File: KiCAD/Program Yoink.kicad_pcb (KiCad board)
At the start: 2 copper layers, 257.2 x 83.3 mm, 123 parts, among them SW1 Rotary_Encoder_Switch, SW2 SW_Push, U1 ATmega32U2-AU, U2 PRTR5V0U2X, Y1 Crystal_GND24_Small

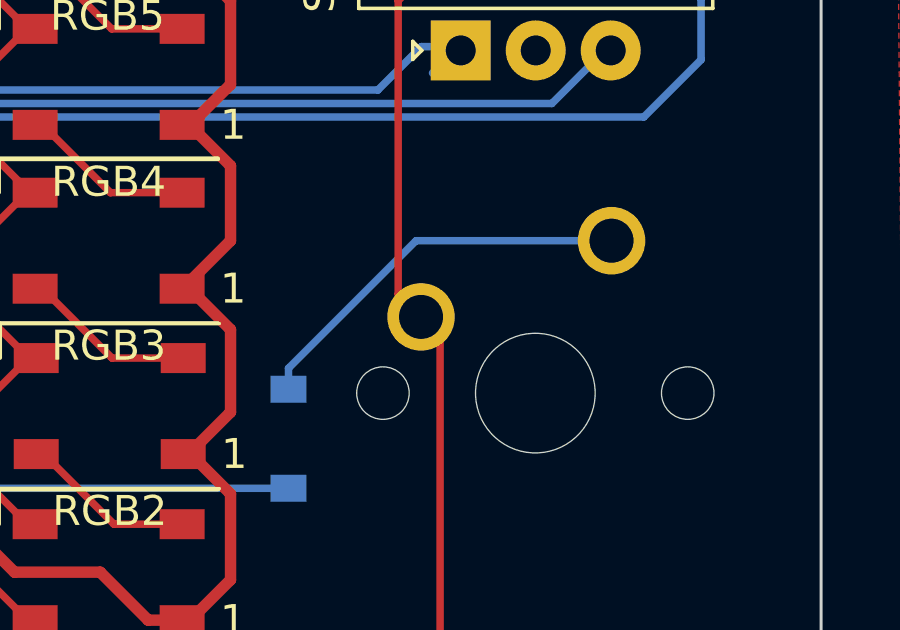
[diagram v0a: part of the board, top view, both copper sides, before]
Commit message: Updated Symbol lib path
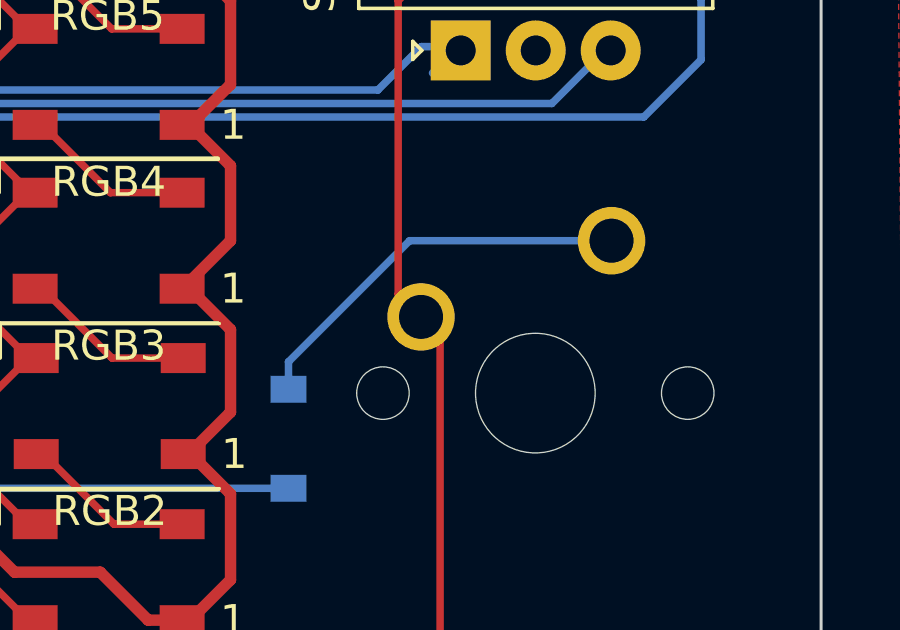
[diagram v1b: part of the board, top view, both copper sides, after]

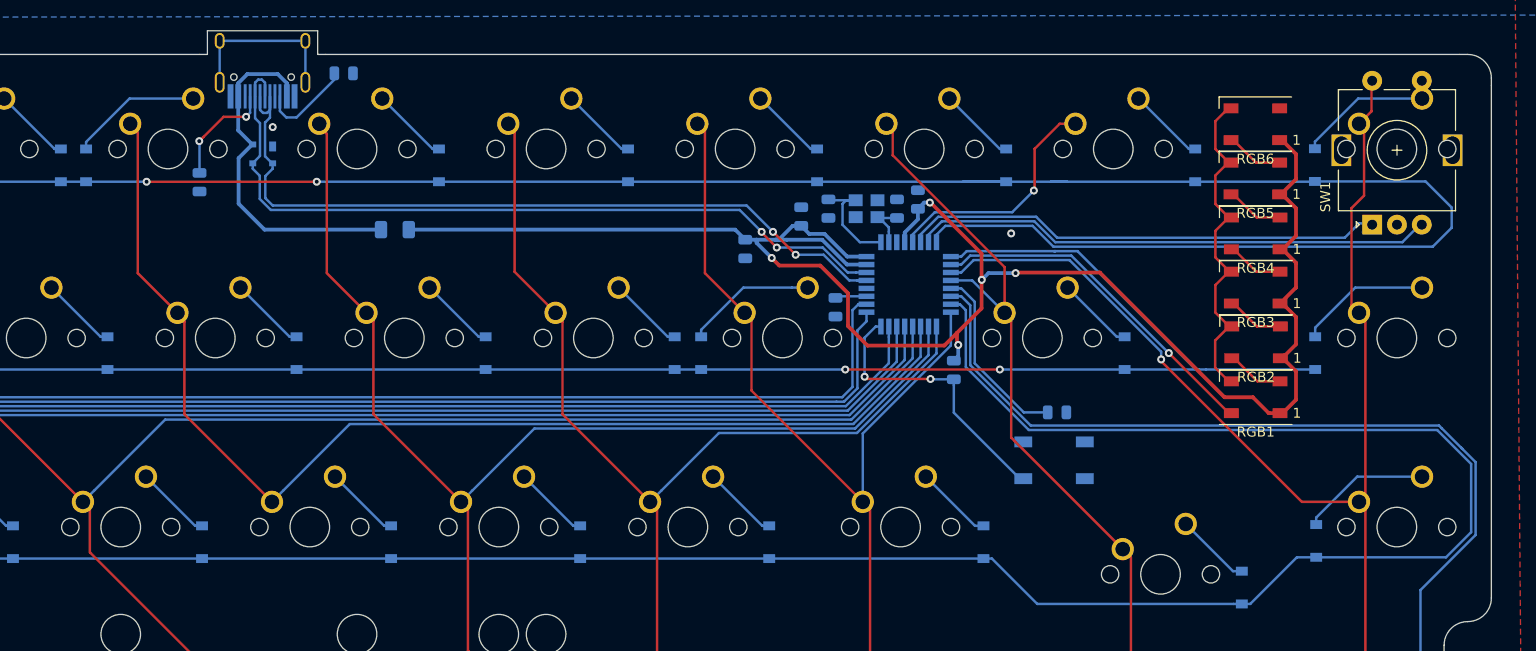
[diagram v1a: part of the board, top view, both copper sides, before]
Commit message: Fixed LED gnd
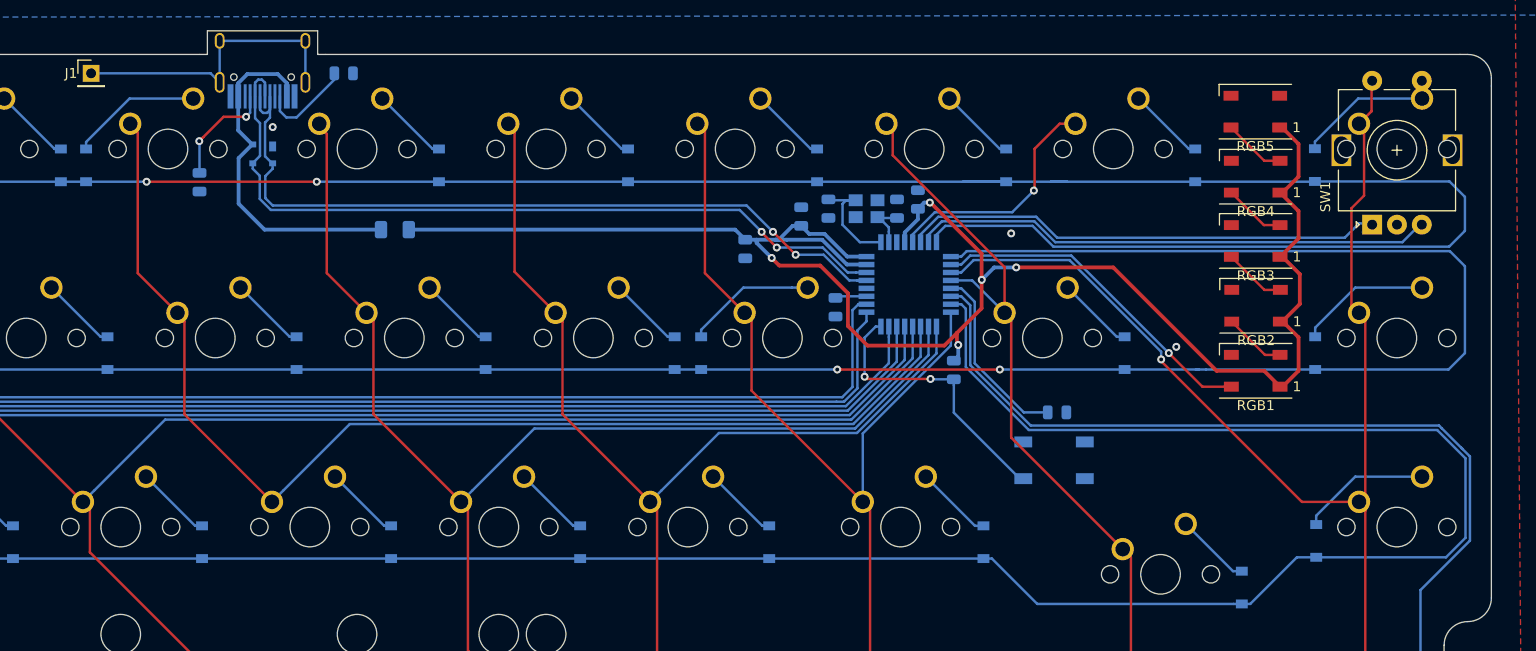
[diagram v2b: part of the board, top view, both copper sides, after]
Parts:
- removed RGB6: WS2812B, LED_SMD:LED_WS2812B_PLCC4_5.0x5.0mm_P3.2mm
- added G***: LOGO, Silk:Program_Yoink_silk_400, F.Cu at (-5.08, -221.1)
- added G***: LOGO, Silk:Program_Yoink_silk_100, F.Cu at (-17.4, -317.0)
- added J1: Conn_01x01, Connector_PinHeader_2.54mm:PinHeader_1x01_P2.54mm_Vertical, F.Cu at (-20.4, -258.4)
- moved RGB5 6.73 mm to (96.9, -254.6)
- moved RGB4 5.72 mm to (96.9, -248.0)
- moved RGB3 4.70 mm to (96.9, -241.6)
- moved RGB2 3.68 mm to (96.9, -235.0)
- moved RGB1 2.67 mm to (96.9, -228.5)
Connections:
- RGB1 pad 3: Net-(RGB1-Pad3) -> GND
- RGB2 pad 3: Net-(RGB1-Pad3) -> GND
- RGB3 pad 3: Net-(RGB1-Pad3) -> GND
- RGB4 pad 3: Net-(RGB1-Pad3) -> GND
- RGB5 pad 3: Net-(RGB1-Pad3) -> GND
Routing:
- net ROW01: track 249.3 -> 296.5 mm
- net Net-(RGB1-Pad3): track 35.4 -> 0.00 mm
- net Net-(J1-Pad1): track 17.0 -> 30.3 mm
- net Net-(RGB5-Pad2): track 5.84 -> 0.00 mm
- net ROW00: track 298.8 -> 302.3 mm
- net +5V: track 183.1 -> 180.6 mm
- net GND: track 0.00 -> 1.00 mm, vias 2 -> 3
- net RGB_PWM: track 35.2 -> 34.4 mm
- net Net-(RGB2-Pad2): track 5.89 -> 6.57 mm
- net Net-(RGB4-Pad2): track 5.91 -> 6.58 mm
- net Net-(RGB3-Pad2): track 5.84 -> 6.51 mm
- net Net-(RGB1-Pad2): track 5.83 -> 6.50 mm
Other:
- board text removed: "PROGRAM YOINK!"

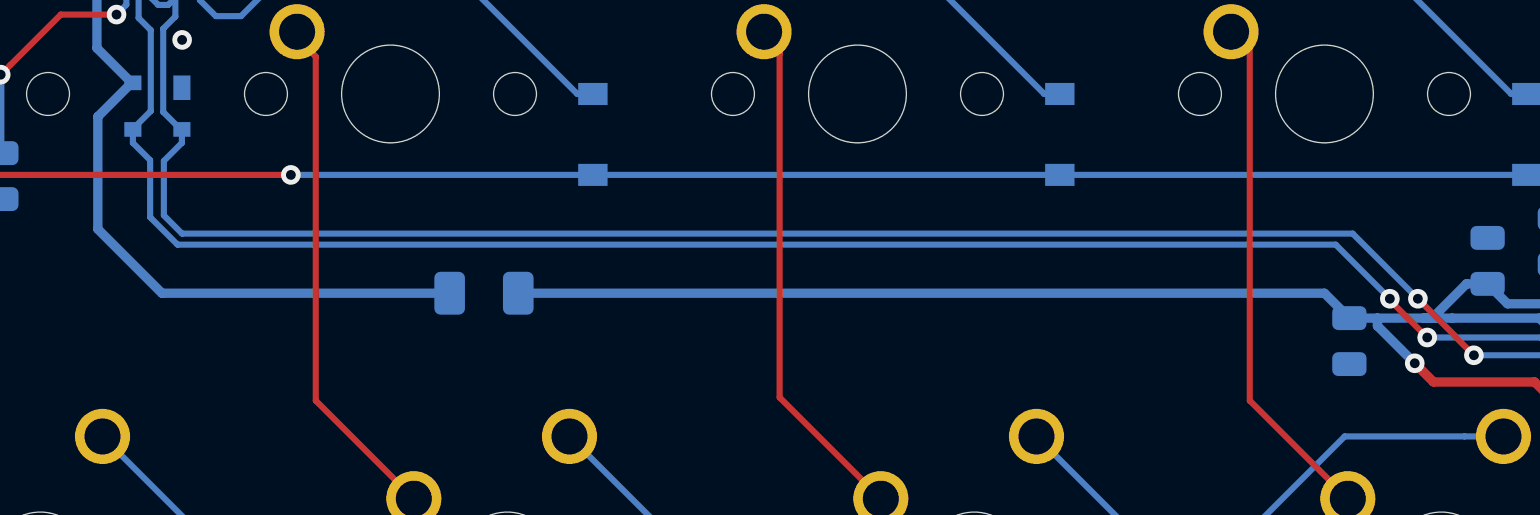
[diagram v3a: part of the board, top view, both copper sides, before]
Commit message: Updated PCB
Added resistors to data lines
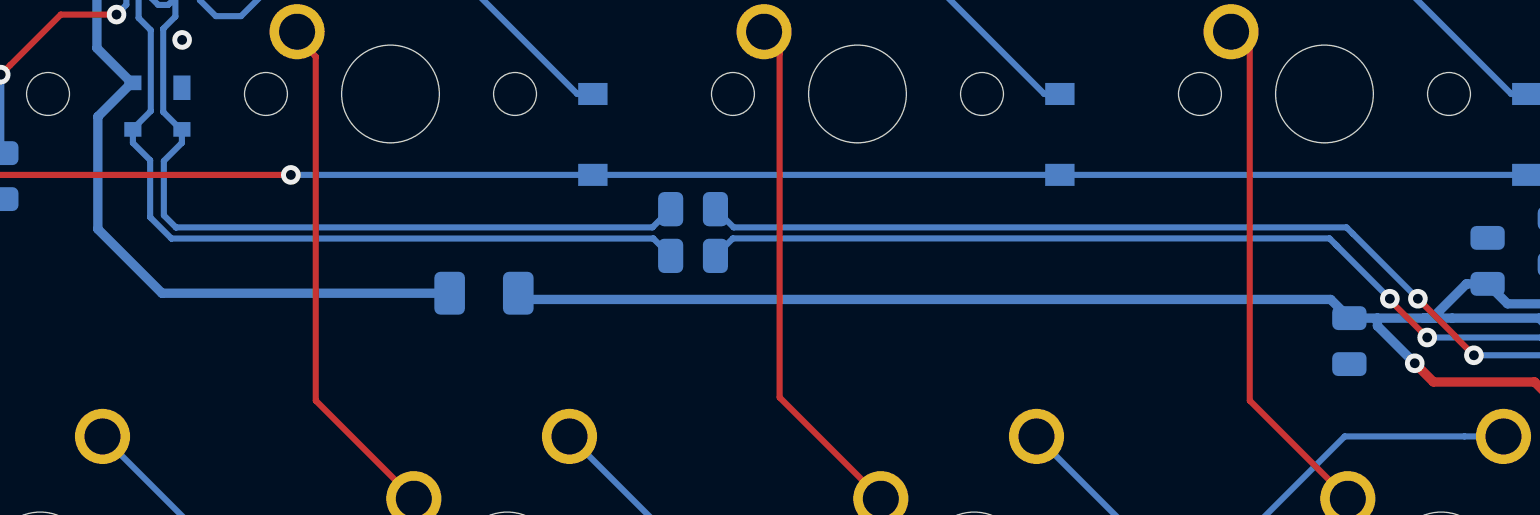
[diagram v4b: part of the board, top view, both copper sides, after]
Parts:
- added R5: 22, Resistor_SMD:R_0805_2012Metric, B.Cu at (18.7, -244.2)
- added R6: 22, Resistor_SMD:R_0805_2012Metric, B.Cu at (18.7, -246.1)
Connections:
- U2 pad 2: D+ -> Net-(R6-Pad2)
- U2 pad 3: D- -> Net-(R5-Pad2)
- USB1 pad 5: D- -> Net-(R5-Pad2)
- USB1 pad 6: D+ -> Net-(R6-Pad2)
- USB1 pad 7: D- -> Net-(R5-Pad2)
- USB1 pad 8: D+ -> Net-(R6-Pad2)
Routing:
- net D-: track 79.4 -> 41.2 mm
- net D+: track 80.1 -> 42.6 mm
- net Net-(R5-Pad2): track 0.00 -> 37.0 mm
- net Net-(R6-Pad2): track 0.00 -> 36.3 mm

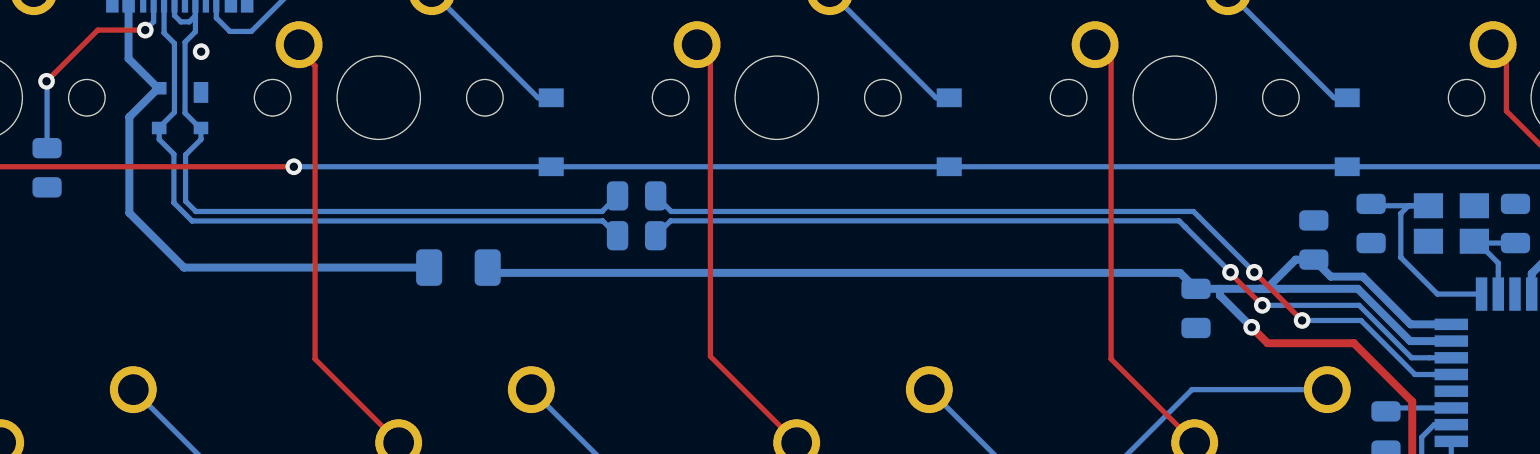
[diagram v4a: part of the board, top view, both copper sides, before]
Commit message: Added data resistors
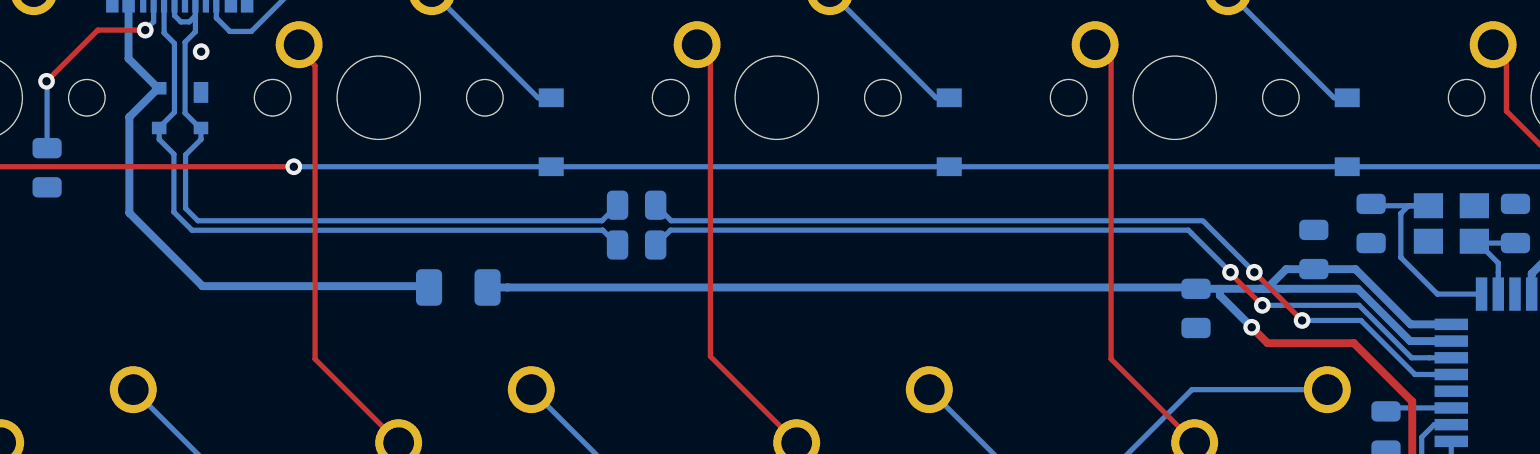
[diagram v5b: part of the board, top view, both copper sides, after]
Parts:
- moved F1 0.95 mm to (10.2, -241.7)
- moved C5 0.45 mm to (51.1, -243.6)
- moved R5 0.44 mm to (18.7, -243.8)
- moved R6 0.44 mm to (18.7, -245.7)
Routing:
- net +5V: track 180.6 -> 179.8 mm

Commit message: Prepared production files
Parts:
- USB1: footprint Type-C:HRO-TYPE-C-31-M-12-HandSoldering -> Type-C:HRO-TYPE-C-31-M-12-Assembly
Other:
- board text added: "SHIELD"
